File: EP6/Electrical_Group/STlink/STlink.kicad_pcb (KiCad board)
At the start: 4 copper layers, 18 x 23.9 mm, 48 parts, among them J1 STDC14, J2 S_SWD, J3 USB_C_stm32, Q1 MMBT3904, U1 XC6206P332MR-G, U2 STM32F103CBT6, U3 LM66100DCK, Y1 8MHz X50328MSB2GI

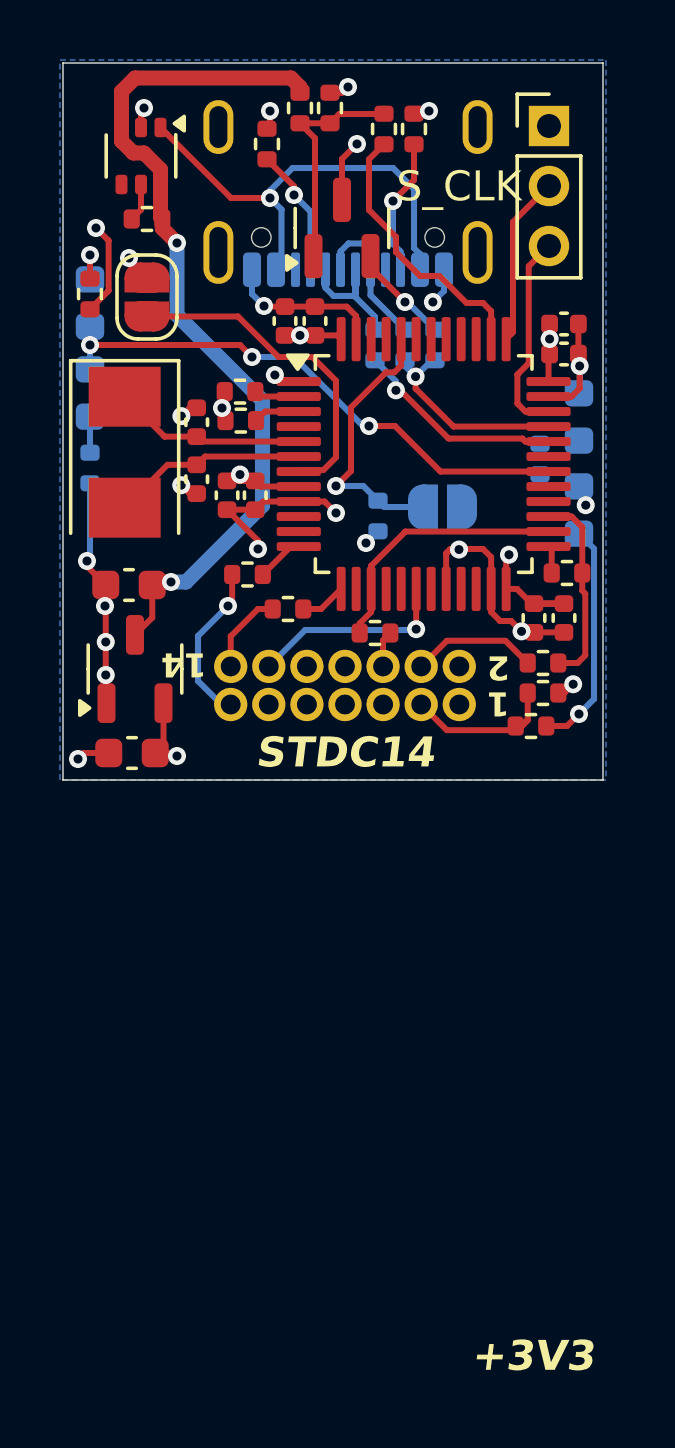
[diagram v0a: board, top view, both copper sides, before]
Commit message: update STlink to V1.1
change to design for self assembly (V1.0 designed for JLCPCBA)
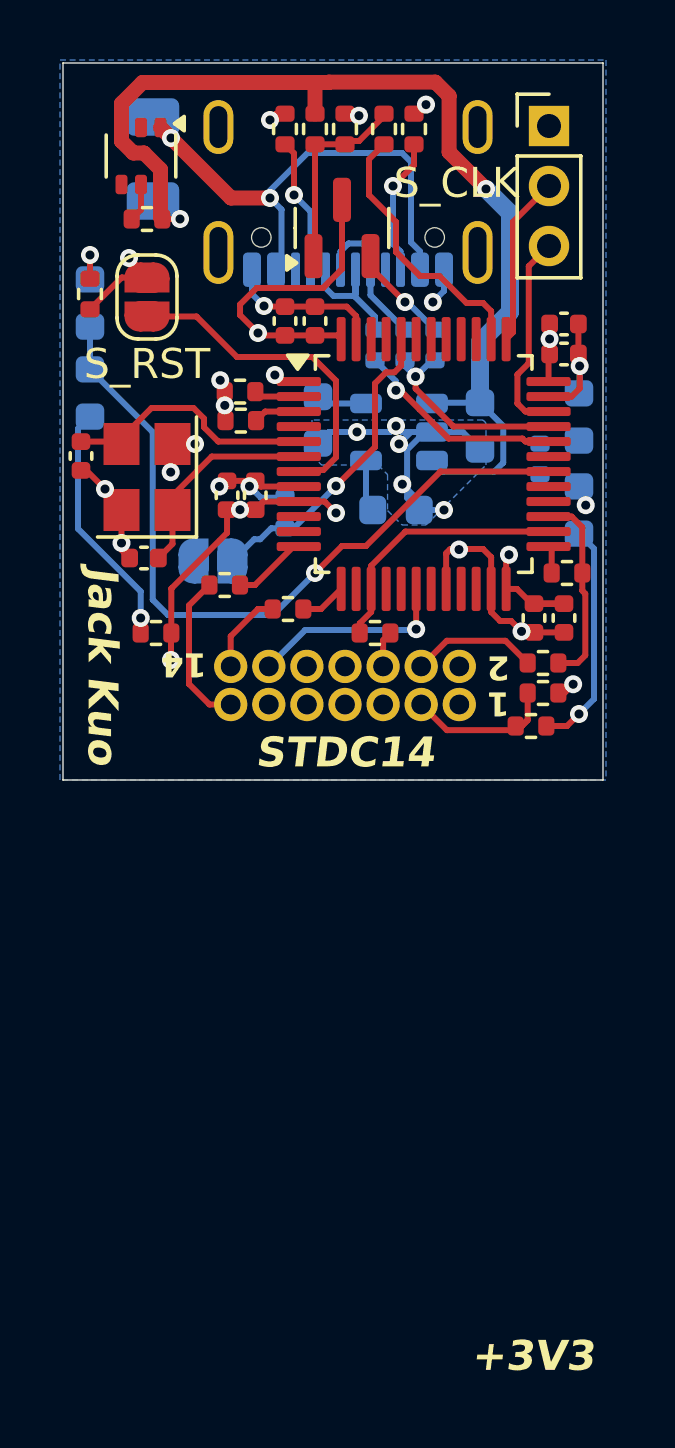
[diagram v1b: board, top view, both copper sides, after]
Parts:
- removed Y1: 8MHz X50328MSB2GI, Crystal:Crystal_SMD_5032-2Pin_5.0x3.2mm
- added C3: 22n, Capacitor_SMD:C_0603_1608Metric, B.Cu at (133.1, 55.4)
- added F1: 0.5A, Fuse:Fuse_1206_3216Metric, B.Cu at (125.0, 43.7)
- added Y2: 8MHz, Crystal:Crystal_SMD_3225-4Pin_3.2x2.5mm, F.Cu at (124.8, 54.3)
- C1, C2: moved to B.Cu
- D3: renamed from D4; value RED led -> GREEN led
- D4: renamed from D3; value GREEN led -> RED led
- R10: renamed from R14; moved to F.Cu
- R23, R24, R5, R6: value 100R -> 20R
- U1: value XC6206P332MR-G -> RT9193; footprint Package_TO_SOT_SMD:SOT-23-3 -> PCM_Package_TO_SOT_SMD_AKL:SOT-23-5; moved to B.Cu
- moved C1 12.8 mm to (135.9, 52.6), turned to -90 degrees
- moved C2 12.7 mm to (130.5, 52.4), turned to -90 degrees
- moved U1 11.8 mm to (133.2, 52.8), turned to 180 degrees
- moved JP2 7.86 mm to (127.0, 57.1)
- moved R10 5.92 mm to (125.1, 59.5), turned to 180 degrees
- moved C12 4.02 mm to (122.6, 53.6), turned to -90 degrees
- moved C13 3.16 mm to (124.7, 57.0), turned to 180 degrees
- moved R11 3.10 mm to (129.4, 55.5), turned to 90 degrees
- moved R17 0.86 mm to (130.4, 42.7)
- moved R19 0.86 mm to (131.4, 42.7)
- moved R5 0.84 mm to (127.4, 57.9)
- moved R20 0.78 mm to (129.4, 42.7)
- turned D3 to -90 degrees
- turned D4 to -90 degrees
- turned R14 to -90 degrees
- renumbered R10 to R14
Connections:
- net /STlinkCore/OSC_IN renamed /STlink/OSC_IN
- net /STlinkCore/OSC_OUT renamed /STlink/OSC_OUT
- net /STlinkCore/RENUM renamed /STlink/RENUM
- net /STlinkCore/S_CLK renamed /STlink/S_CLK
- net /STlinkCore/S_DIO renamed /STlink/S_DIO
- net /STlinkCore/S_NRST renamed /STlink/S_NRST
- net /STlinkCore/T_SWO renamed /STlink/T_SWO
- net /STlinkCore/USART2_RX renamed /STlink/USART2_RX
- net /STlinkCore/USART2_TX renamed /STlink/USART2_TX
- net /STlinkCore/USB_D+ renamed /STlink/USB_D+
- net /STlinkCore/USB_D- renamed /STlink/USB_D-
- net /STlinkCore/USB_DN renamed /STlink/USB_DN
- net /STlinkCore/USB_DP renamed /STlink/USB_DP
- net /STlinkCore/VBUS renamed /STlink/VBUS
- net /STlinkCore/t_CLK renamed /STlink/t_CLK
- net /STlinkCore/t_DIO renamed /STlink/t_DIO
- D3 pad 1: Net-(D4-K) -> /STlink/LED_STLINK
- D3 pad 2: /STlinkCore/LED_STLINK -> Net-(D3-A)
- D4 pad 1: /STlinkCore/LED_STLINK -> Net-(D4-K)
- D4 pad 2: Net-(D3-A) -> /STlink/LED_STLINK
- JP2 pad 1: +3V3 -> /STlink/BOOT0
- JP2 pad 2: /STlinkCore/BOOT0 -> +3V3
- R10 pad 1: Net-(D4-K) -> +3V3
- R10 pad 2: GND -> Net-(D3-A)
- R11 pad 1: /STlinkCore/BOOT0 -> /STlink/BOOT0
- R14 pad 1: +3V3 -> Net-(D4-K)
- R14 pad 2: Net-(D3-A) -> GND
- U1 pad 1: GND -> +5V
- U1 pad 2: +3V3 -> GND
- U2 pad 30: /STlinkCore/LED_STLINK -> /STlink/LED_STLINK
- U2 pad 44: /STlinkCore/BOOT0 -> /STlink/BOOT0
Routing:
- net /STlink/LED_STLINK: track 0.00 -> 25.4 mm, vias 0 -> 1
- net /STlinkCore/LED_STLINK: track 19.1 -> 0.00 mm, vias 3 -> 0
- net /STlink/BOOT0: track 0.00 -> 10.4 mm, vias 0 -> 1
- net GND: track 39.1 -> 48.4 mm, vias 21 -> 23
- net /STlinkCore/BOOT0: track 9.15 -> 0.00 mm, vias 1 -> 0
- net +5V: track 29.1 -> 36.9 mm
- net +3V3: track 23.1 -> 30.3 mm, vias 10 -> 8
- net Net-(D3-A): track 1.60 -> 8.24 mm
- net /STlink/OSC_IN: track 6.42 -> 8.54 mm
- net /STlink/VBUS: track 15.7 -> 17.5 mm, vias 1 -> 2
- net Net-(U1-BYP): track 0.00 -> 1.74 mm
- net Net-(Q1-B): track 7.59 -> 6.52 mm
- net /STlink/USART2_TX: track 1.59 -> 2.49 mm
- net /STlink/OSC_OUT: track 6.51 -> 7.02 mm
- net Net-(D4-K): track 1.20 -> 1.60 mm, vias 0 -> 1
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- added copper zone on B.Cu, net GND
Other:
- board text added: "EP6 STlink"
- board text added: "FUSE"
- board text added: "Jack Kuo"
- board text added: "S_RST"
- board text added: "V1.1 25/05/04"
- board text removed: "EP6 Jack Kuo"
- board text removed: "STlink V1.0 25/05/04"

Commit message: update STlink to V1.2
only add fillet
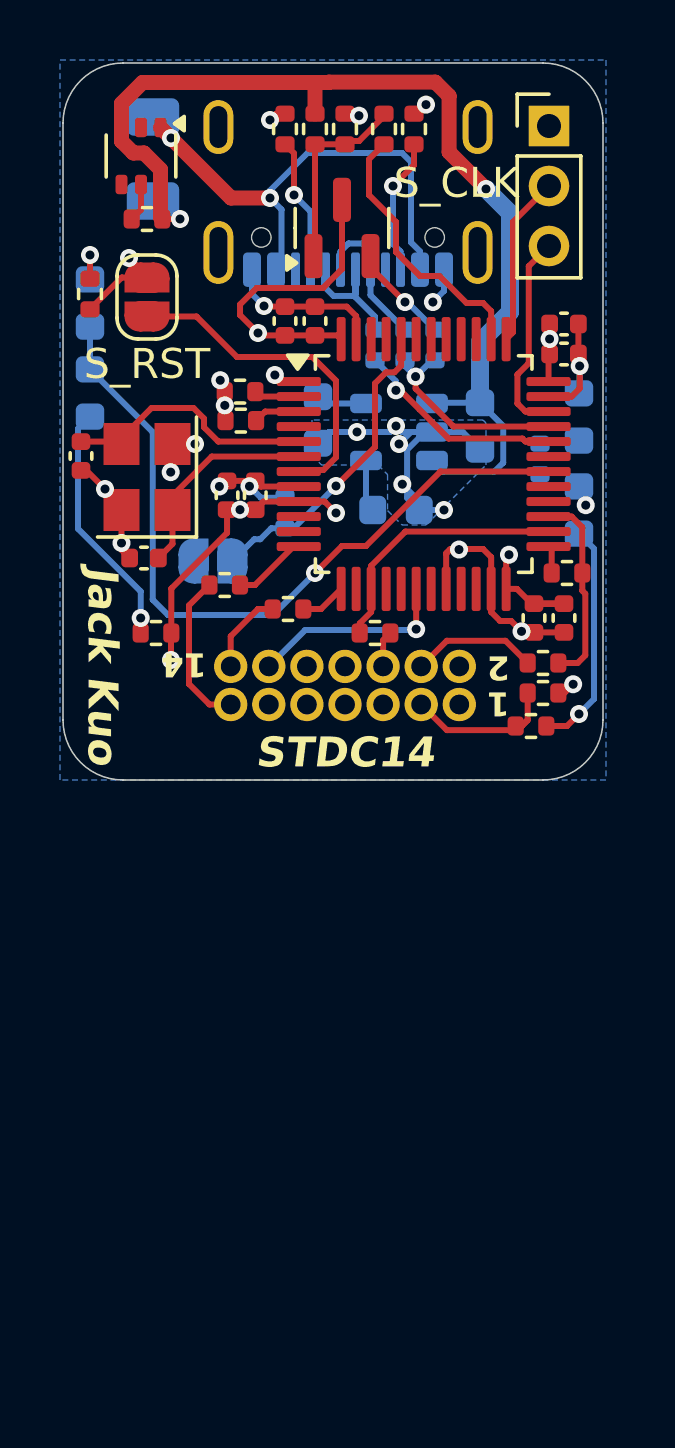
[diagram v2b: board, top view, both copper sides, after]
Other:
- outline, holes or cut-outs redrawn
- board text removed: "+3V3"
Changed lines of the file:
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@@
 	(title_block
 		(title "STlink")
-		(date "2025-05-04")
-		(rev "1.1")
+		(date "2025-05-09")
+		(rev "1.2")
 		(company "NTURacing")
 		(comment 1 "Jack Kuo")
@@
 		(tags "capacitor")
 		(property "Reference" "C13"
-			(at 0 -1.16 360)
+			(at 0 -1.16 0)
 			(layer "F.SilkS")
 			(hide yes)
@@
 		)
 		(property "Value" "30p"
-			(at 0 1.16 360)
+			(at 0 1.16 0)
 			(layer "F.Fab")
 			(effects
@@
 		)
 		(fp_text user "${REFERENCE}"
-			(at 0 0 360)
+			(at 0 0 0)
 			(layer "F.Fab")
 			(effects
@@
 		)
 	)
-	(gr_rect
-		(start 122 40.5)
-		(end 140 64.4)
+	(gr_line
+		(start 122 62.4)
+		(end 122 42.5)
+		(stroke
+			(width 0.05)
+			(type default)
+		)
+		(layer "Edge.Cuts")
+	)
+	(gr_arc
+		(start 124 64.4)
+		(mid 122.585786 63.814214)
+		(end 122 62.4)
+		(stroke
+			(width 0.05)
+			(type default)
+		)
+		(layer "Edge.Cuts")
+	)
+	(gr_line
+		(start 124 40.5)
+		(end 138 40.5)
+		(stroke
+			(width 0.05)
+			(type default)
+		)
+		(layer "Edge.Cuts")
+	)
+	(gr_arc
+		(start 122 42.5)
+		(mid 122.585786 41.085786)
+		(end 124 40.5)
+		(stroke
+			(width 0.05)
+			(type default)
+		)
+		(layer "Edge.Cuts")
+	)
+	(gr_line
+		(start 138 64.4)
+		(end 124 64.4)
+		(stroke
+			(width 0.05)
+			(type default)
+		)
+		(layer "Edge.Cuts")
+	)
+	(gr_line
+		(start 140 42.5)
+		(end 140 62.4)
+		(stroke
+			(width 0.05)
+			(type default)
+		)
+		(layer "Edge.Cuts")
+	)
+	(gr_arc
+		(start 140 62.4)
+		(mid 139.414214 63.814214)
+		(end 138 64.4)
+		(stroke
+			(width 0.05)
+			(type default)
+		)
+		(layer "Edge.Cuts")
+	)
+	(gr_arc
+		(start 138 40.5)
+		(mid 139.414214 41.085786)
+		(end 140 42.5)
 		(stroke
 			(width 0.05)
 			(type default)
 		)
-		(fill none)
 		(layer "Edge.Cuts")
 	)
@@
 		)
 	)
-	(gr_text "+3V3"
-		(at 135.6 83.6 0)
-		(layer "F.SilkS")
-		(effects
-			(font
-				(size 1 1)
-				(thickness 0.2)
-				(bold yes)
-				(italic yes)
-			)
-			(justify left)
-		)
-	)
